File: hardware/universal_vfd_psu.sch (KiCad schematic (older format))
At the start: 28 parts, among them U1 LM2733YMF, U2 LM4871MX_NOPB

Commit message: further psu layout optimizations
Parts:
- U2: footprint snapeda_lib:SOIC127P599X175-8N -> Package_SO:SOIC-8_3.9x4.9mm_P1.27mm
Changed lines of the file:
@@
 F 0 "U2" H 7550 4220 50  0000 C CNN
 F 1 "LM4871MX_NOPB" H 7550 4129 50  0000 C CNN
-F 2 "snapeda_lib:SOIC127P599X175-8N" H 7550 3550 50  0001 L BNN
-F 3 "" H 7550 3550 50  0001 C CNN
+F 2 "Package_SO:SOIC-8_3.9x4.9mm_P1.27mm" H 7550 3550 50  0001 L BNN
+F 3 "https://www.ti.com/lit/ds/symlink/lm4871.pdf?HQS=TI-null-null-digikeymode-df-pf-null-wwe&ts=1595529775354" H 7550 3550 50  0001 C CNN
 	1    7550 3550
 	1    0    0    -1

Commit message: commit the board version that went to aisler, more silkscreen info
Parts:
- renumbered U1 to U3
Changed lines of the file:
@@
 $EndDescr
 $Comp
-L Regulator_Switching:LM2733YMF U1
+L Regulator_Switching:LM2733YMF U3
 U 1 1 5F189D50
 P 2450 3400
-F 0 "U1" H 2450 3767 50  0000 C CNN
+F 0 "U3" H 2450 3767 50  0000 C CNN
 F 1 "LM2733YMF" H 2450 3676 50  0000 C CNN
 F 2 "Package_TO_SOT_SMD:SOT-23-5" H 2500 3150 50  0001 L CIN

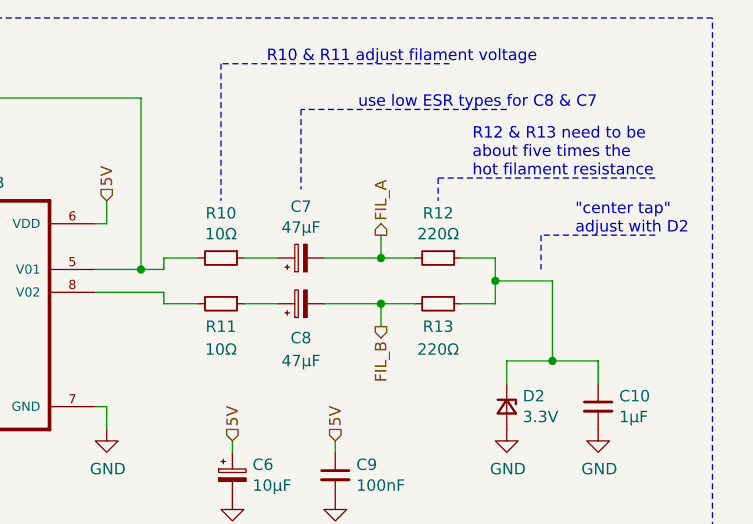
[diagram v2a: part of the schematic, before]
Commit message: update vfddriver resistor values, 10 ohm is too dark, 4.7 too bright
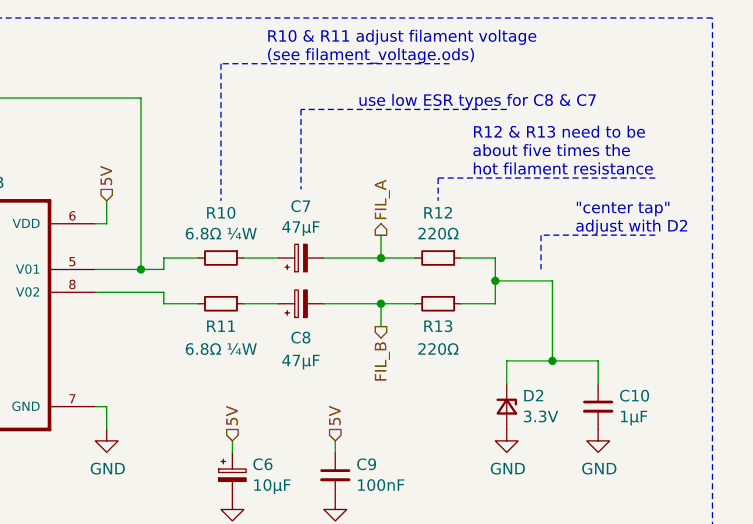
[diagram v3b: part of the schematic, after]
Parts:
- R10, R11: value 10Ω -> 6.8Ω ¼W
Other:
- note added: "R10 & R11 adjust filament voltage\n(see filament_voltage.ods)"
- note removed: "R10 & R11 adjust filament voltage"
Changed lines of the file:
@@
 P 8800 3300
 F 0 "R10" V 8604 3300 50  0000 C CNN
-F 1 "10Ω" V 8695 3300 50  0000 C CNN
+F 1 "6.8Ω ¼W" V 8695 3300 50  0000 C CNN
 F 2 "Resistor_SMD:R_1206_3216Metric_Pad1.42x1.75mm_HandSolder" H 8800 3300 50  0001 C CNN
 F 3 "~" H 8800 3300 50  0001 C CNN
@@
 P 8800 3500
 F 0 "R11" V 8900 3500 50  0000 C CNN
-F 1 "10Ω" V 9000 3500 50  0000 C CNN
+F 1 "6.8Ω ¼W" V 9000 3500 50  0000 C CNN
 F 2 "Resistor_SMD:R_1206_3216Metric_Pad1.42x1.75mm_HandSolder" H 8800 3500 50  0001 C CNN
 F 3 "~" H 8800 3500 50  0001 C CNN
@@
 	6750 4500 6750 4550
 Text Notes 9000 2450 0    50   ~ 0
-R10 & R11 adjust filament voltage
+R10 & R11 adjust filament voltage\n(see filament_voltage.ods)
 Wire Notes Line
 	9800 2450 8800 2450

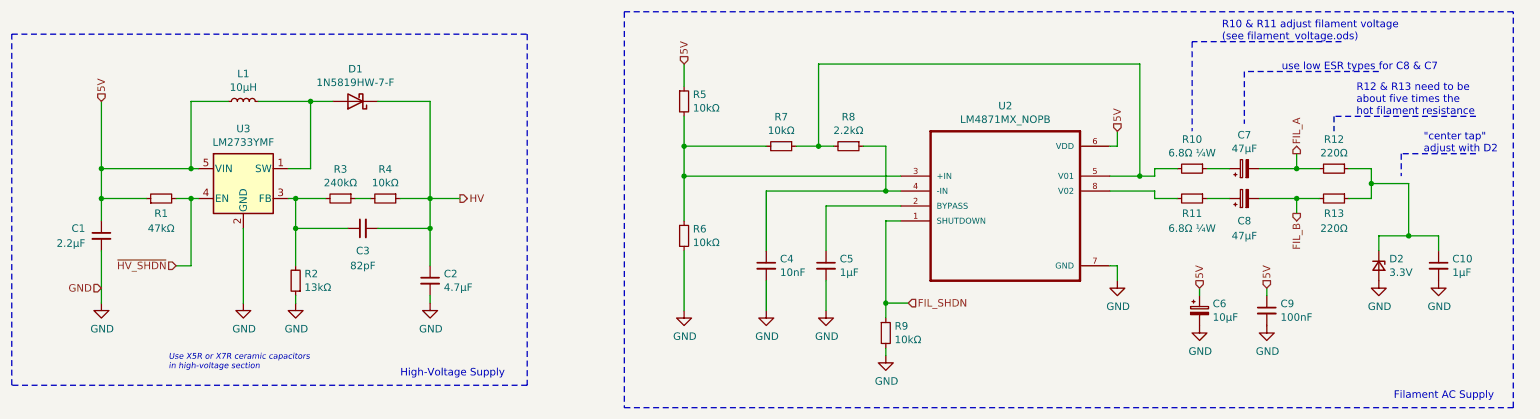
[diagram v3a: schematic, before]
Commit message: hardware: tidy up, fix photodiode, (re)export (i)boms and schematics
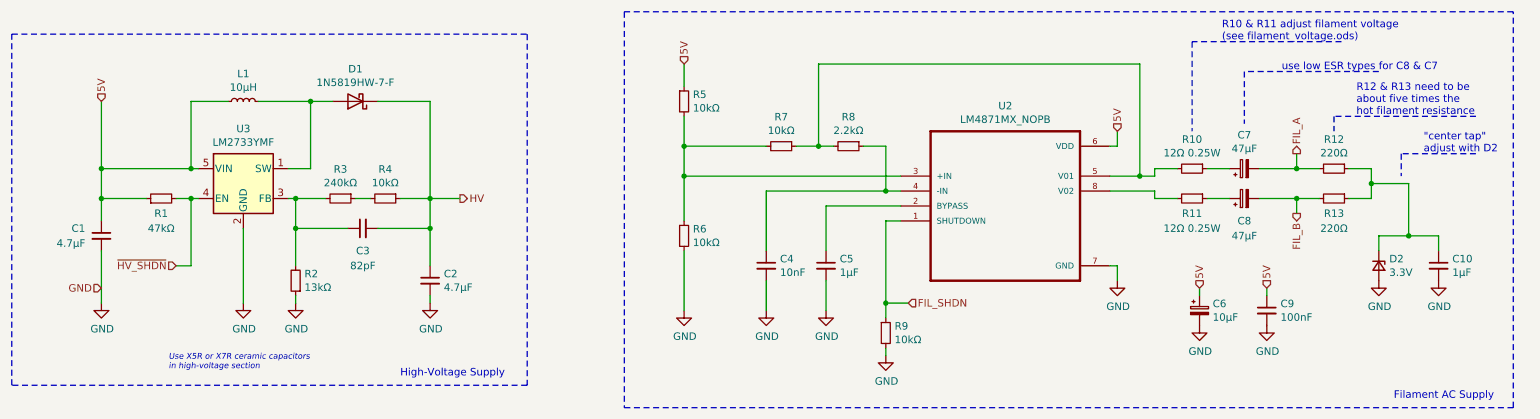
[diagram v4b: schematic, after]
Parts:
- C1: value 2.2µF -> 4.7µF; Digi-Key PN (none) -> 587-5485-1-ND; MPN (none) -> UMK212BBJ475KG-T; Mfg (none) -> Taiyo Yuden
- C10, C5: Digi-Key PN (none) -> 1276-6469-1-ND; MPN (none) -> CL21B105KAFNNNG; Mfg (none) -> Samsung
- C2: Digi-Key PN (none) -> 587-5485-1-ND; MPN (none) -> UMK212BBJ475KG-T; Mfg (none) -> Taiyo Yuden
- C3: Digi-Key PN (none) -> 311-1110-1-ND; MPN (none) -> CC0805JRNPO9BN820; Mfg (none) -> Yageo
- C4: Digi-Key PN (none) -> 311-1136-1-ND; MPN (none) -> CC0805KRX7R9BB103; Mfg (none) -> Yageo
- C6: Digi-Key PN (none) -> 493-2100-1-ND; MPN (none) -> UWX1C100MCL1GB; Mfg (none) -> Nichicon
- C7, C8: Digi-Key PN (none) -> 493-6385-1-ND; MPN (none) -> UCD1E470MCL1GS; Mfg (none) -> Nichicon
- C9: Digi-Key PN (none) -> 1276-1099-1-ND; MPN (none) -> CL21B104KACNNNC; Mfg (none) -> Samsung
- D1: Digi-Key PN (none) -> 1N5819HW-FDICT-ND; MPN (none) -> 1N5819HW-7-F; Mfg (none) -> Diodes Inc.
- D2: Digi-Key PN (none) -> MMSZ4684T1GOSCT-ND; MPN (none) -> MMSZ4684T1G; Mfg (none) -> ON Semi
- L1: Digi-Key PN (none) -> 587-6332-1-ND; MPN (none) -> LBC3225T100MR; Mfg (none) -> Taiyo Yuden
- R1: Digi-Key PN (none) -> 311-47.0KCRCT-ND; MPN (none) -> RC0805FR-0747KL; Mfg (none) -> Yageo
- R10, R11: value 6.8Ω ¼W -> 12Ω 0.25W; Digi-Key PN (none) -> 311-10.0FRCT-ND; MPN (none) -> RC1206FR-0710RL; Mfg (none) -> Yageo
- R12, R13: Digi-Key PN (none) -> 311-220CRCT-ND; MPN (none) -> RC0805FR-07220RL; Mfg (none) -> Yageo
- R2: Digi-Key PN (none) -> 311-13.0KCRCT-ND; MPN (none) -> RC0805FR-0713KL; Mfg (none) -> Yageo
- R3: Digi-Key PN (none) -> 311-240KCRCT-ND; MPN (none) -> RC0805FR-07240KL; Mfg (none) -> Yageo
- R4, R5, R6, R7, R9: Digi-Key PN (none) -> 311-10.0KCRCT-ND; MPN (none) -> RC0805FR-0710KL; Mfg (none) -> Yageo
- R8: Digi-Key PN (none) -> 311-2.20KCRCT-ND; MPN (none) -> RC0805FR-072K2L; Mfg (none) -> Yageo
- U2: Digi-Key PN (none) -> LM4871MX/NOPBCT-ND; MPN (none) -> LM4871MX/NOPB; Mfg (none) -> Texas Instr
- U3: Digi-Key PN (none) -> LM2733YMF/NOPBCT-ND; MPN (none) -> LM2733YMF/NOPB; Mfg (none) -> Texas Instr
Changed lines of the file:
@@
 F 2 "Package_TO_SOT_SMD:SOT-23-5" H 2500 3150 50  0001 L CIN
 F 3 "http://www.ti.com/lit/ds/symlink/lm2733.pdf" H 2450 3500 50  0001 C CNN
+F 4 "LM2733YMF/NOPBCT-ND" H 2450 3400 50  0001 C CNN "Digi-Key PN"
+F 5 "LM2733YMF/NOPB" H 2450 3400 50  0001 C CNN "MPN"
+F 6 "Texas Instr" H 2450 3400 50  0001 C CNN "Mfg"
 	1    2450 3400
 	1    0    0    -1
@@
 P 1500 3750
 F 0 "C1" H 1300 3800 50  0000 L CNN
-F 1 "2.2µF" H 1200 3700 50  0000 L CNN
+F 1 "4.7µF" H 1200 3700 50  0000 L CNN
 F 2 "Capacitor_SMD:C_0805_2012Metric_Pad1.15x1.40mm_HandSolder" H 1500 3750 50  0001 C CNN
 F 3 "~" H 1500 3750 50  0001 C CNN
+F 4 "587-5485-1-ND" H 1500 3750 50  0001 C CNN "Digi-Key PN"
+F 5 "UMK212BBJ475KG-T" H 1500 3750 50  0001 C CNN "MPN"
+F 6 "Taiyo Yuden" H 1500 3750 50  0001 C CNN "Mfg"
 	1    1500 3750
 	1    0    0    -1
@@
 F 2 "Capacitor_SMD:C_0805_2012Metric_Pad1.15x1.40mm_HandSolder" H 3700 4050 50  0001 C CNN
 F 3 "~" H 3700 4050 50  0001 C CNN
+F 4 "587-5485-1-ND" H 3700 4050 50  0001 C CNN "Digi-Key PN"
+F 5 "UMK212BBJ475KG-T" H 3700 4050 50  0001 C CNN "MPN"
+F 6 "Taiyo Yuden" H 3700 4050 50  0001 C CNN "Mfg"
 	1    3700 4050
 	1    0    0    -1
@@
 F 2 "Capacitor_SMD:C_0805_2012Metric_Pad1.15x1.40mm_HandSolder" H 3250 3700 50  0001 C CNN
 F 3 "~" H 3250 3700 50  0001 C CNN
+F 4 "311-1110-1-ND" H 3250 3700 50  0001 C CNN "Digi-Key PN"
+F 5 "CC0805JRNPO9BN820" H 3250 3700 50  0001 C CNN "MPN"
+F 6 "Yageo" H 3250 3700 50  0001 C CNN "Mfg"
 	1    3250 3700
 	0    -1   -1   0
@@
 F 2 "Resistor_SMD:R_0805_2012Metric_Pad1.15x1.40mm_HandSolder" H 3100 3500 50  0001 C CNN
 F 3 "~" H 3100 3500 50  0001 C CNN
+F 4 "311-240KCRCT-ND" H 3100 3500 50  0001 C CNN "Digi-Key PN"
+F 5 "RC0805FR-07240KL" H 3100 3500 50  0001 C CNN "MPN"
+F 6 "Yageo" H 3100 3500 50  0001 C CNN "Mfg"
 	1    3100 3500
 	0    1    1    0
@@
 F 2 "Resistor_SMD:R_0805_2012Metric_Pad1.15x1.40mm_HandSolder" H 3400 3500 50  0001 C CNN
 F 3 "~" H 3400 3500 50  0001 C CNN
+F 4 "311-10.0KCRCT-ND" H 3400 3500 50  0001 C CNN "Digi-Key PN"
+F 5 "RC0805FR-0710KL" H 3400 3500 50  0001 C CNN "MPN"
+F 6 "Yageo" H 3400 3500 50  0001 C CNN "Mfg"
 	1    3400 3500
 	0    1    1    0
@@
 F 2 "Resistor_SMD:R_0805_2012Metric_Pad1.15x1.40mm_HandSolder" H 2800 4050 50  0001 C CNN
 F 3 "~" H 2800 4050 50  0001 C CNN
+F 4 "311-13.0KCRCT-ND" H 2800 4050 50  0001 C CNN "Digi-Key PN"
+F 5 "RC0805FR-0713KL" H 2800 4050 50  0001 C CNN "MPN"
+F 6 "Yageo" H 2800 4050 50  0001 C CNN "Mfg"
 	1    2800 4050
 	-1   0    0    1
@@
 F 2 "Resistor_SMD:R_0805_2012Metric_Pad1.15x1.40mm_HandSolder" H 1900 3500 50  0001 C CNN
 F 3 "~" H 1900 3500 50  0001 C CNN
+F 4 "311-47.0KCRCT-ND" H 1900 3500 50  0001 C CNN "Digi-Key PN"
+F 5 "RC0805FR-0747KL" H 1900 3500 50  0001 C CNN "MPN"
+F 6 "Yageo" H 1900 3500 50  0001 C CNN "Mfg"
 	1    1900 3500
 	0    -1   -1   0
@@
 F 2 "Inductor_SMD:L_1210_3225Metric_Pad1.42x2.65mm_HandSolder" H 2450 2850 50  0001 C CNN
 F 3 "https://ds.yuden.co.jp/TYCOMPAS/ut/detail?pn=LBC3225T100MR%20%20&u=M" H 2450 2850 50  0001 C CNN
+F 4 "587-6332-1-ND" H 2450 2850 50  0001 C CNN "Digi-Key PN"
+F 5 "LBC3225T100MR" H 2450 2850 50  0001 C CNN "MPN"
+F 6 "Taiyo Yuden" H 2450 2850 50  0001 C CNN "Mfg"
 	1    2450 2850
 	0    -1   -1   0
@@
 F 2 "Diode_SMD:D_SOD-123" H 3200 2675 50  0001 C CNN
 F 3 "https://www.diodes.com/assets/Datasheets/ds30217.pdf" H 3200 2850 50  0001 C CNN
+F 4 "1N5819HW-FDICT-ND" H 3200 2850 50  0001 C CNN "Digi-Key PN"
+F 5 "1N5819HW-7-F" H 3200 2850 50  0001 C CNN "MPN"
+F 6 "Diodes Inc." H 3200 2850 50  0001 C CNN "Mfg"
 	1    3200 2850
 	-1   0    0    1
@@
 F 2 "Package_SO:SOIC-8_3.9x4.9mm_P1.27mm" H 7550 3550 50  0001 L BNN
 F 3 "https://www.ti.com/lit/ds/symlink/lm4871.pdf?HQS=TI-null-null-digikeymode-df-pf-null-wwe&ts=1595529775354" H 7550 3550 50  0001 C CNN
+F 4 "LM4871MX/NOPBCT-ND" H 7550 3550 50  0001 C CNN "Digi-Key PN"
+F 5 "LM4871MX/NOPB" H 7550 3550 50  0001 C CNN "MPN"
+F 6 "Texas Instr" H 7550 3550 50  0001 C CNN "Mfg"
 	1    7550 3550
 	1    0    0    -1
@@
 F 2 "Capacitor_SMD:C_0805_2012Metric_Pad1.15x1.40mm_HandSolder" H 6350 3950 50  0001 C CNN
 F 3 "~" H 6350 3950 50  0001 C CNN
+F 4 "1276-6469-1-ND" H 6350 3950 50  0001 C CNN "Digi-Key PN"
+F 5 "CL21B105KAFNNNG" H 6350 3950 50  0001 C CNN "MPN"
+F 6 "Samsung" H 6350 3950 50  0001 C CNN "Mfg"
 	1    6350 3950
 	1    0    0    -1
@@
 F 2 "Capacitor_SMD:C_0805_2012Metric_Pad1.15x1.40mm_HandSolder" H 5950 3950 50  0001 C CNN
 F 3 "~" H 5950 3950 50  0001 C CNN
+F 4 "311-1136-1-ND" H 5950 3950 50  0001 C CNN "Digi-Key PN"
+F 5 "CC0805KRX7R9BB103" H 5950 3950 50  0001 C CNN "MPN"
+F 6 "Yageo" H 5950 3950 50  0001 C CNN "Mfg"
 	1    5950 3950
 	1    0    0    -1
@@
 F 2 "Resistor_SMD:R_0805_2012Metric_Pad1.15x1.40mm_HandSolder" H 6750 4400 50  0001 C CNN
 F 3 "~" H 6750 4400 50  0001 C CNN
+F 4 "311-10.0KCRCT-ND" H 6750 4400 50  0001 C CNN "Digi-Key PN"
+F 5 "RC0805FR-0710KL" H 6750 4400 50  0001 C CNN "MPN"
+F 6 "Yageo" H 6750 4400 50  0001 C CNN "Mfg"
 	1    6750 4400
 	1    0    0    -1
@@
 F 2 "Resistor_SMD:R_0805_2012Metric_Pad1.15x1.40mm_HandSolder" H 5400 3750 50  0001 C CNN
 F 3 "~" H 5400 3750 50  0001 C CNN
+F 4 "311-10.0KCRCT-ND" H 5400 3750 50  0001 C CNN "Digi-Key PN"
+F 5 "RC0805FR-0710KL" H 5400 3750 50  0001 C CNN "MPN"
+F 6 "Yageo" H 5400 3750 50  0001 C CNN "Mfg"
 	1    5400 3750
 	1    0    0    -1
@@
 F 2 "Resistor_SMD:R_0805_2012Metric_Pad1.15x1.40mm_HandSolder" H 5400 2850 50  0001 C CNN
 F 3 "~" H 5400 2850 50  0001 C CNN
+F 4 "311-10.0KCRCT-ND" H 5400 2850 50  0001 C CNN "Digi-Key PN"
+F 5 "RC0805FR-0710KL" H 5400 2850 50  0001 C CNN "MPN"
+F 6 "Yageo" H 5400 2850 50  0001 C CNN "Mfg"
 	1    5400 2850
 	1    0    0    -1
@@
 F 2 "Resistor_SMD:R_0805_2012Metric_Pad1.15x1.40mm_HandSolder" H 6500 3150 50  0001 C CNN
 F 3 "~" H 6500 3150 50  0001 C CNN
+F 4 "311-2.20KCRCT-ND" H 6500 3150 50  0001 C CNN "Digi-Key PN"
+F 5 "RC0805FR-072K2L" H 6500 3150 50  0001 C CNN "MPN"
+F 6 "Yageo" H 6500 3150 50  0001 C CNN "Mfg"
 	1    6500 3150
 	0    1    1    0
@@
 F 2 "Resistor_SMD:R_0805_2012Metric_Pad1.15x1.40mm_HandSolder" H 6050 3150 50  0001 C CNN
 F 3 "~" H 6050 3150 50  0001 C CNN
+F 4 "311-10.0KCRCT-ND" H 6050 3150 50  0001 C CNN "Digi-Key PN"
+F 5 "RC0805FR-0710KL" H 6050 3150 50  0001 C CNN "MPN"
+F 6 "Yageo" H 6050 3150 50  0001 C CNN "Mfg"
 	1    6050 3150
 	0    1    1    0
@@
 F 2 "Capacitor_SMD:CP_Elec_6.3x5.9" H 9150 3300 50  0001 C CNN
 F 3 "~" H 9150 3300 50  0001 C CNN
+F 4 "493-6385-1-ND" H 9150 3300 50  0001 C CNN "Digi-Key PN"
+F 5 "UCD1E470MCL1GS" H 9150 3300 50  0001 C CNN "MPN"
+F 6 "Nichicon" H 9150 3300 50  0001 C CNN "Mfg"
 	1    9150 3300
 	0    -1   -1   0
@@
 F 2 "Capacitor_SMD:CP_Elec_6.3x5.9" H 9150 3500 50  0001 C CNN
 F 3 "~" H 9150 3500 50  0001 C CNN
+F 4 "493-6385-1-ND" H 9150 3500 50  0001 C CNN "Digi-Key PN"
+F 5 "UCD1E470MCL1GS" H 9150 3500 50  0001 C CNN "MPN"
+F 6 "Nichicon" H 9150 3500 50  0001 C CNN "Mfg"
 	1    9150 3500
 	0    -1   -1   0
@@
 P 8800 3300
 F 0 "R10" V 8604 3300 50  0000 C CNN
-F 1 "6.8Ω ¼W" V 8695 3300 50  0000 C CNN
+F 1 "12Ω 0.25W" V 8695 3300 50  0000 C CNN
 F 2 "Resistor_SMD:R_1206_3216Metric_Pad1.42x1.75mm_HandSolder" H 8800 3300 50  0001 C CNN
 F 3 "~" H 8800 3300 50  0001 C CNN
+F 4 "311-10.0FRCT-ND" H 8800 3300 50  0001 C CNN "Digi-Key PN"
+F 5 "RC1206FR-0710RL" H 8800 3300 50  0001 C CNN "MPN"
+F 6 "Yageo" H 8800 3300 50  0001 C CNN "Mfg"
 	1    8800 3300
 	0    1    1    0
@@
 P 8800 3500
 F 0 "R11" V 8900 3500 50  0000 C CNN
-F 1 "6.8Ω ¼W" V 9000 3500 50  0000 C CNN
+F 1 "12Ω 0.25W" V 9000 3500 50  0000 C CNN
 F 2 "Resistor_SMD:R_1206_3216Metric_Pad1.42x1.75mm_HandSolder" H 8800 3500 50  0001 C CNN
 F 3 "~" H 8800 3500 50  0001 C CNN
+F 4 "311-10.0FRCT-ND" H 8800 3500 50  0001 C CNN "Digi-Key PN"
+F 5 "RC1206FR-0710RL" H 8800 3500 50  0001 C CNN "MPN"
+F 6 "Yageo" H 8800 3500 50  0001 C CNN "Mfg"
 	1    8800 3500
 	0    1    1    0
@@
 F 2 "Resistor_SMD:R_0805_2012Metric_Pad1.15x1.40mm_HandSolder" H 9750 3500 50  0001 C CNN
 F 3 "~" H 9750 3500 50  0001 C CNN
+F 4 "311-220CRCT-ND" H 9750 3500 50  0001 C CNN "Digi-Key PN"
+F 5 "RC0805FR-07220RL" H 9750 3500 50  0001 C CNN "MPN"
+F 6 "Yageo" H 9750 3500 50  0001 C CNN "Mfg"
 	1    9750 3500
 	0    1    1    0
@@
 F 2 "Resistor_SMD:R_0805_2012Metric_Pad1.15x1.40mm_HandSolder" H 9750 3300 50  0001 C CNN
 F 3 "~" H 9750 3300 50  0001 C CNN
+F 4 "311-220CRCT-ND" H 9750 3300 50  0001 C CNN "Digi-Key PN"
+F 5 "RC0805FR-07220RL" H 9750 3300 50  0001 C CNN "MPN"
+F 6 "Yageo" H 9750 3300 50  0001 C CNN "Mfg"
 	1    9750 3300
 	0    1    1    0
@@
 F 2 "Diode_SMD:D_SOD-123" V 10050 3950 50  0001 C CNN
 F 3 "~" V 10050 3950 50  0001 C CNN
+F 4 "MMSZ4684T1GOSCT-ND" H 10050 3950 50  0001 C CNN "Digi-Key PN"
+F 5 "MMSZ4684T1G" H 10050 3950 50  0001 C CNN "MPN"
+F 6 "ON Semi" H 10050 3950 50  0001 C CNN "Mfg"
 	1    10050 3950
 	0    1    1    0
@@
 F 2 "Capacitor_SMD:C_0805_2012Metric_Pad1.15x1.40mm_HandSolder" H 10450 3950 50  0001 C CNN
 F 3 "~" H 10450 3950 50  0001 C CNN
+F 4 "1276-6469-1-ND" H 10450 3950 50  0001 C CNN "Digi-Key PN"
+F 5 "CL21B105KAFNNNG" H 10450 3950 50  0001 C CNN "MPN"
+F 6 "Samsung" H 10450 3950 50  0001 C CNN "Mfg"
 	1    10450 3950
 	1    0    0    -1
@@
 F 2 "Capacitor_SMD:CP_Elec_4x5.4" H 8850 4250 50  0001 C CNN
 F 3 "~" H 8850 4250 50  0001 C CNN
+F 4 "493-2100-1-ND" H 8850 4250 50  0001 C CNN "Digi-Key PN"
+F 5 "UWX1C100MCL1GB" H 8850 4250 50  0001 C CNN "MPN"
+F 6 "Nichicon" H 8850 4250 50  0001 C CNN "Mfg"
 	1    8850 4250
 	1    0    0    -1
@@
 F 2 "Capacitor_SMD:C_0805_2012Metric_Pad1.15x1.40mm_HandSolder" H 9300 4250 50  0001 C CNN
 F 3 "~" H 9300 4250 50  0001 C CNN
+F 4 "1276-1099-1-ND" H 9300 4250 50  0001 C CNN "Digi-Key PN"
+F 5 "CL21B104KACNNNC" H 9300 4250 50  0001 C CNN "MPN"
+F 6 "Samsung" H 9300 4250 50  0001 C CNN "Mfg"
 	1    9300 4250
 	1    0    0    -1
